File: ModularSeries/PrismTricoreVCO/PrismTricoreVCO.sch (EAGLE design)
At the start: 56 parts, among them IC1 LM13700_DIP, IC2 TL084P, IC3 TL084P, Q1 2N3906, Q2 2N3906

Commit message: Prism files added, readme updated
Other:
- note added: "Prism Triangle Core Voltage Controlled Oscillator Aidan Taylor 2020 ELECTRIC NOODLE BOX"
- note removed: "Triangle Core Voltage Controlled Oscillator Aidan Taylor 2020 ELECTRIC NOODLE BOX"
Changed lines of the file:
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@@
 <text x="81.28" y="139.7" size="1.778" layer="97" align="center">Q1 and Q2 are a matched to within 1.5mV Vbe
 and are in physical contact with R16</text>
-<text x="-45.72" y="22.86" size="2.54" layer="97" align="center-left">Triangle Core Voltage Controlled Oscillator
+<text x="-45.72" y="22.86" size="2.54" layer="97" align="center-left">Prism
+Triangle Core Voltage Controlled Oscillator
 Aidan Taylor 2020
 ELECTRIC NOODLE BOX</text>

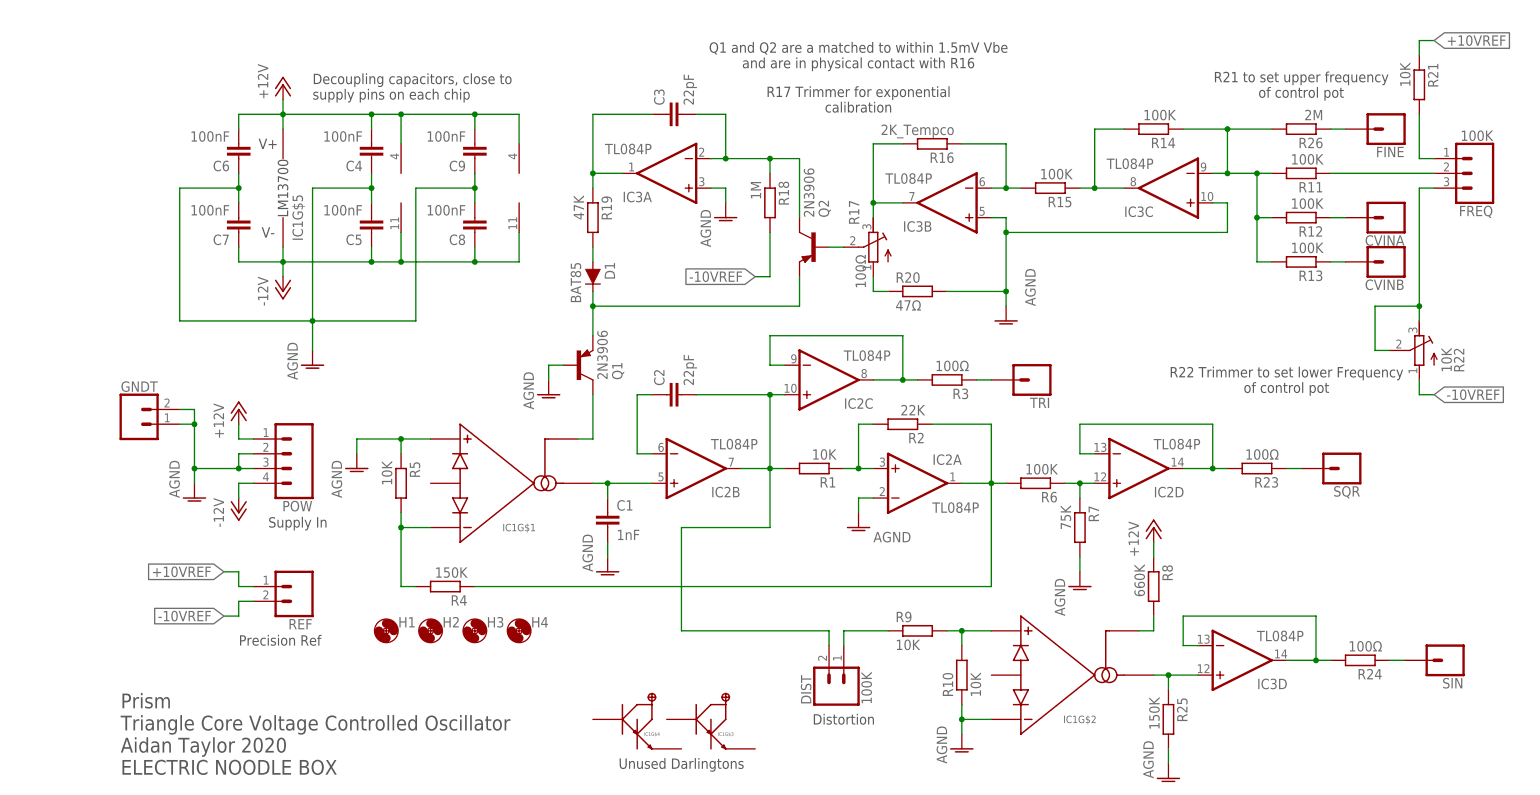
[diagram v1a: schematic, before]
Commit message: All PCBs now use unified library, Eagle library added
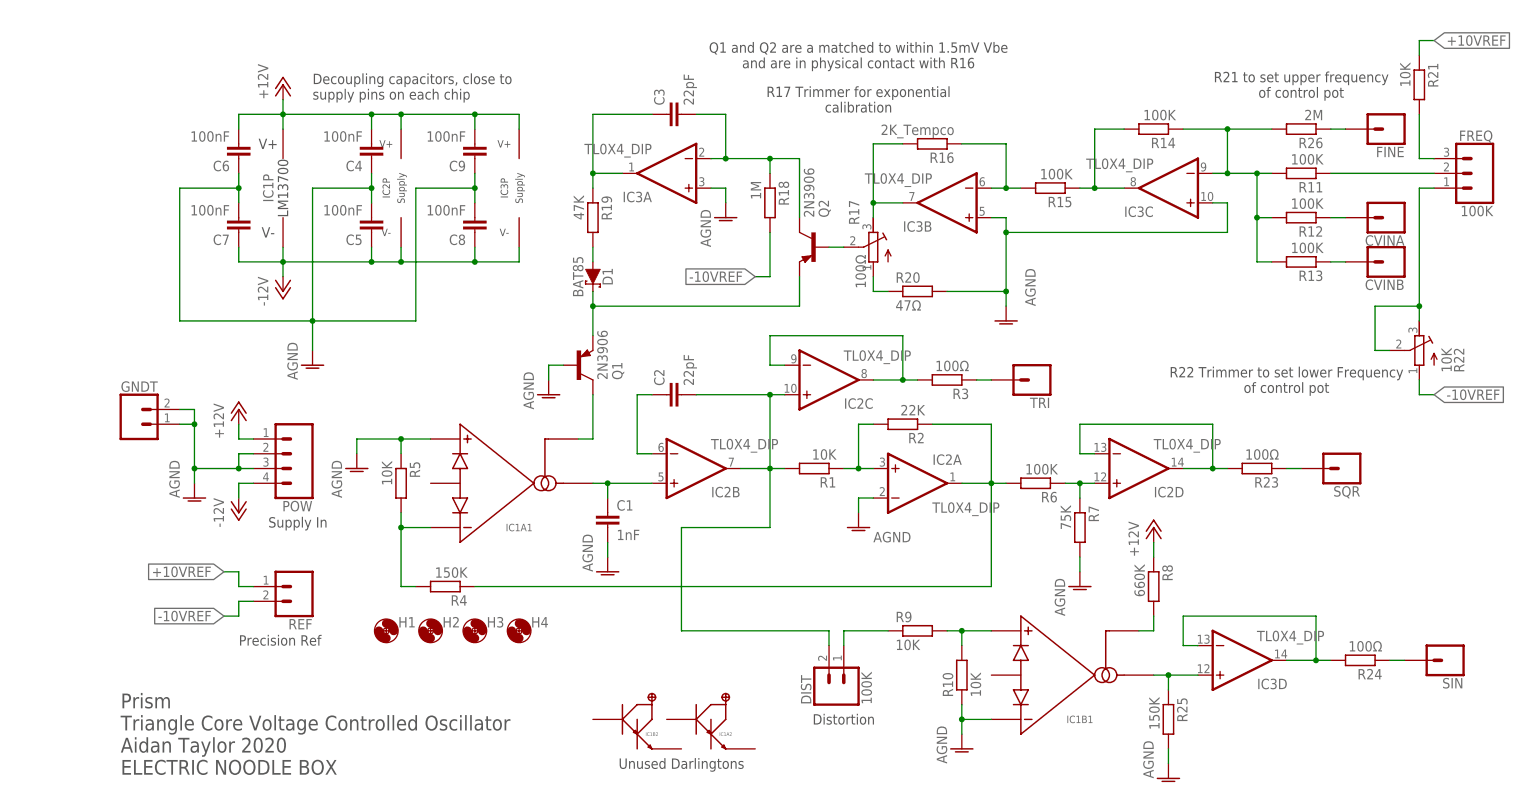
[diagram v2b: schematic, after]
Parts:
- CVINA, CVINB, FINE, SIN, SQR, TRI: value (none) -> 1XWIREPAD; device SparkFun-Connectors:CONN_01 -> ElectricNoodleBox:1XWIREPAD
- D1: device SparkFun-DiscreteSemi:DIODE-1N4148 -> ElectricNoodleBox:SCHOTTKY_DO35
- DIST: device SparkFun-Connectors:CONN_02 -> ElectricNoodleBox:2XWIREPAD
- FREQ: device SparkFun-Connectors:CONN_03 -> ElectricNoodleBox:3XWIREPAD
- GNDT: value (none) -> 2XWIREPAD; device SparkFun-Connectors:CONN_02 -> ElectricNoodleBox:2XWIREPAD
- IC1: device ElectricNoodleBox2018:LM13700_DIP -> ElectricNoodleBox:LM13700_DIP
- IC2, IC3: value TL084P -> TL0X4_DIP; device linear:TL084P -> ElectricNoodleBox:TL0X4_DIP
- POW: value (none) -> 4XMOLEX; device SparkFun-Connectors:CONN_04POLAR -> ElectricNoodleBox:4XMOLEX
- REF: value (none) -> 2XMOLEX; device SparkFun-Connectors:CONN_02POLAR -> ElectricNoodleBox:2XMOLEX
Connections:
- net +12V: now also IC1P.V+; no longer IC1G$5.V+
- net -12V: now also IC1P.V-; no longer IC1G$5.V-
- net AGND: now also IC1A1.AMP+, IC1B1.AMP-; no longer IC1G$1.AMP+, IC1G$2.AMP-
- net N$10: now also IC1B1.AMPOUT; no longer IC1G$2.AMPOUT
- net N$11: now also IC1B1.AMPBIAS; no longer IC1G$2.AMPBIAS
- net N$12: now also IC1A1.AMPBIAS; no longer IC1G$1.AMPBIAS
- net N$25: now also FREQ.1; no longer FREQ.3
- net N$26: now also FREQ.3; no longer FREQ.1
- net N$4: now also IC1A1.AMPOUT; no longer IC1G$1.AMPOUT
- net N$7: now also IC1A1.AMP-; no longer IC1G$1.AMP-
- net N$8: now also IC1B1.AMP+; no longer IC1G$2.AMP+

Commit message: C2 removed from Prism
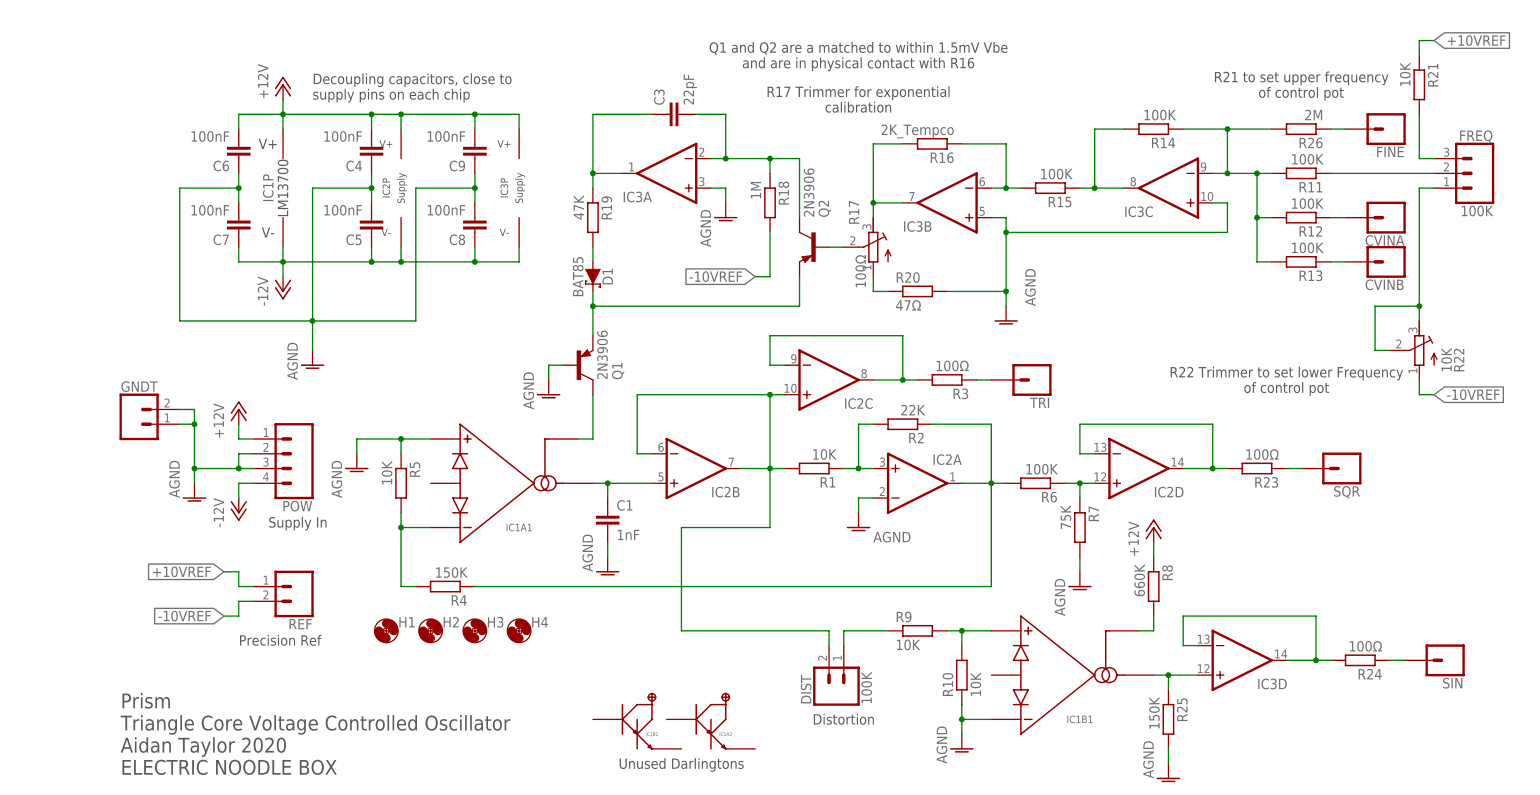
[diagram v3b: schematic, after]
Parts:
- removed C2: 22pF, rcl:C-EU050-025X075
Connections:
- removed net N$2: C2.2, DIST.2, IC2B.OUT, IC2C.+IN, R1.2
- net N$1: now also DIST.2, IC2B.OUT, IC2C.+IN, R1.2; no longer C2.1
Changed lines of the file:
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@@
 <part name="AGND1" library="supply1" library_urn="urn:adsk.eagle:library:371" deviceset="AGND" device=""/>
 <part name="AGND3" library="supply1" library_urn="urn:adsk.eagle:library:371" deviceset="AGND" device=""/>
-<part name="C2" library="rcl" library_urn="urn:adsk.eagle:library:334" deviceset="C-EU" device="050-025X075" package3d_urn="urn:adsk.eagle:package:23637/1" value="22pF"/>
 <part name="R2" library="rcl" library_urn="urn:adsk.eagle:library:334" deviceset="R-EU_" device="0207/10" package3d_urn="urn:adsk.eagle:package:23491/2" value="22K"/>
 <part name="R3" library="rcl" library_urn="urn:adsk.eagle:library:334" deviceset="R-EU_" device="0207/10" package3d_urn="urn:adsk.eagle:package:23491/2" value="100Ω"/>
@@
 <instance part="IC2" gate="B" x="53.34" y="68.58" smashed="yes" rot="MR180">
 <attribute name="NAME" x="55.88" y="65.405" size="1.778" layer="95" rot="MR180"/>
-<attribute name="VALUE" x="55.88" y="73.66" size="1.778" layer="96" rot="MR180"/>
 </instance>
 <instance part="IC2" gate="C" x="76.2" y="83.82" smashed="yes" rot="MR180">
 <attribute name="NAME" x="78.74" y="80.645" size="1.778" layer="95" rot="MR180"/>
-<attribute name="VALUE" x="78.74" y="88.9" size="1.778" layer="96" rot="MR180"/>
 </instance>
 <instance part="IC2" gate="A" x="91.44" y="66.04" smashed="yes">
 <attribute name="NAME" x="93.98" y="69.215" size="1.778" layer="95"/>
-<attribute name="VALUE" x="93.98" y="60.96" size="1.778" layer="96"/>
 </instance>
 <instance part="IC2" gate="D" x="129.54" y="68.58" smashed="yes" rot="MR180">
 <attribute name="NAME" x="132.08" y="65.405" size="1.778" layer="95" rot="MR180"/>
-<attribute name="VALUE" x="132.08" y="73.66" size="1.778" layer="96" rot="MR180"/>
 </instance>
 <instance part="IC2" gate="P" x="2.54" y="116.84" smashed="yes">
@@
 <attribute name="VALUE" x="83.82" y="55.88" size="1.778" layer="96"/>
 </instance>
-<instance part="C2" gate="G$1" x="48.26" y="81.28" smashed="yes" rot="R90">
-<attribute name="NAME" x="47.879" y="82.804" size="1.778" layer="95" rot="R90"/>
-<attribute name="VALUE" x="52.959" y="82.804" size="1.778" layer="96" rot="R90"/>
-</instance>
 <instance part="R2" gate="G$1" x="88.9" y="76.2" smashed="yes" rot="R180">
 <attribute name="NAME" x="92.71" y="74.7014" size="1.778" layer="95" rot="R180"/>
@@
 <instance part="IC3" gate="D" x="147.32" y="35.56" smashed="yes" rot="MR180">
 <attribute name="NAME" x="149.86" y="32.385" size="1.778" layer="95" rot="MR180"/>
-<attribute name="VALUE" x="149.86" y="40.64" size="1.778" layer="96" rot="MR180"/>
 </instance>
 <instance part="IC3" gate="C" x="134.62" y="116.84" smashed="yes" rot="R180">
 <attribute name="NAME" x="132.08" y="113.665" size="1.778" layer="95" rot="R180"/>
-<attribute name="VALUE" x="132.08" y="121.92" size="1.778" layer="96" rot="R180"/>
 </instance>
 <instance part="IC3" gate="B" x="96.52" y="114.3" smashed="yes" rot="R180">
 <attribute name="NAME" x="93.98" y="111.125" size="1.778" layer="95" rot="R180"/>
-<attribute name="VALUE" x="93.98" y="119.38" size="1.778" layer="96" rot="R180"/>
 </instance>
 <instance part="IC3" gate="A" x="48.26" y="119.38" smashed="yes" rot="R180">
 <attribute name="NAME" x="45.72" y="116.205" size="1.778" layer="95" rot="R180"/>
-<attribute name="VALUE" x="45.72" y="124.46" size="1.778" layer="96" rot="R180"/>
 </instance>
 <instance part="IC3" gate="P" x="22.86" y="116.84" smashed="yes">
@@
 <wire x1="45.72" y1="71.12" x2="43.18" y2="71.12" width="0.1524" layer="91"/>
 <wire x1="43.18" y1="71.12" x2="43.18" y2="81.28" width="0.1524" layer="91"/>
-<pinref part="C2" gate="G$1" pin="1"/>
-<wire x1="43.18" y1="81.28" x2="45.72" y2="81.28" width="0.1524" layer="91"/>
-</segment>
-</net>
-<net name="N$2" class="0">
-<segment>
-<pinref part="C2" gate="G$1" pin="2"/>
-<wire x1="53.34" y1="81.28" x2="66.04" y2="81.28" width="0.1524" layer="91"/>
+<wire x1="43.18" y1="81.28" x2="66.04" y2="81.28" width="0.1524" layer="91"/>
 <wire x1="66.04" y1="81.28" x2="66.04" y2="68.58" width="0.1524" layer="91"/>
 <pinref part="IC2" gate="B" pin="OUT"/>

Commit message: Library updated, variants consolidated
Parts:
- IC1: value LM13700_DIP -> (none); device ElectricNoodleBox:LM13700_DIP -> ElectricNoodleBox:LM13700DIL
- IC2, IC3: value TL0X4_DIP -> (none); device ElectricNoodleBox:TL0X4_DIP -> ElectricNoodleBox:TL0X4DIL
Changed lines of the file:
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@@
 </classes>
 <parts>
-<part name="IC1" library="ElectricNoodleBox" deviceset="LM13700_DIP" device="" package3d_urn="urn:adsk.eagle:package:922/2"/>
-<part name="IC2" library="ElectricNoodleBox" deviceset="TL0X4_DIP" device="" package3d_urn="urn:adsk.eagle:package:16407/2"/>
+<part name="IC1" library="ElectricNoodleBox" deviceset="LM13700" device="DIL" package3d_urn="urn:adsk.eagle:package:922/2"/>
+<part name="IC2" library="ElectricNoodleBox" deviceset="TL0X4" device="DIL" package3d_urn="urn:adsk.eagle:package:16407/2"/>
 <part name="R1" library="rcl" library_urn="urn:adsk.eagle:library:334" deviceset="R-EU_" device="0207/10" package3d_urn="urn:adsk.eagle:package:23491/2" value="10K"/>
 <part name="C1" library="rcl" library_urn="urn:adsk.eagle:library:334" deviceset="C-EU" device="050-025X075" package3d_urn="urn:adsk.eagle:package:23637/1" value="1nF"/>
@@
 <part name="AGND2" library="supply1" library_urn="urn:adsk.eagle:library:371" deviceset="AGND" device=""/>
 <part name="P+1" library="supply1" library_urn="urn:adsk.eagle:library:371" deviceset="+12V" device=""/>
-<part name="IC3" library="ElectricNoodleBox" deviceset="TL0X4_DIP" device="" package3d_urn="urn:adsk.eagle:package:16407/2"/>
+<part name="IC3" library="ElectricNoodleBox" deviceset="TL0X4" device="DIL" package3d_urn="urn:adsk.eagle:package:16407/2"/>
 <part name="R11" library="rcl" library_urn="urn:adsk.eagle:library:334" deviceset="R-EU_" device="0207/10" package3d_urn="urn:adsk.eagle:package:23491/2" value="100K"/>
 <part name="R12" library="rcl" library_urn="urn:adsk.eagle:library:334" deviceset="R-EU_" device="0207/10" package3d_urn="urn:adsk.eagle:package:23491/2" value="100K"/>

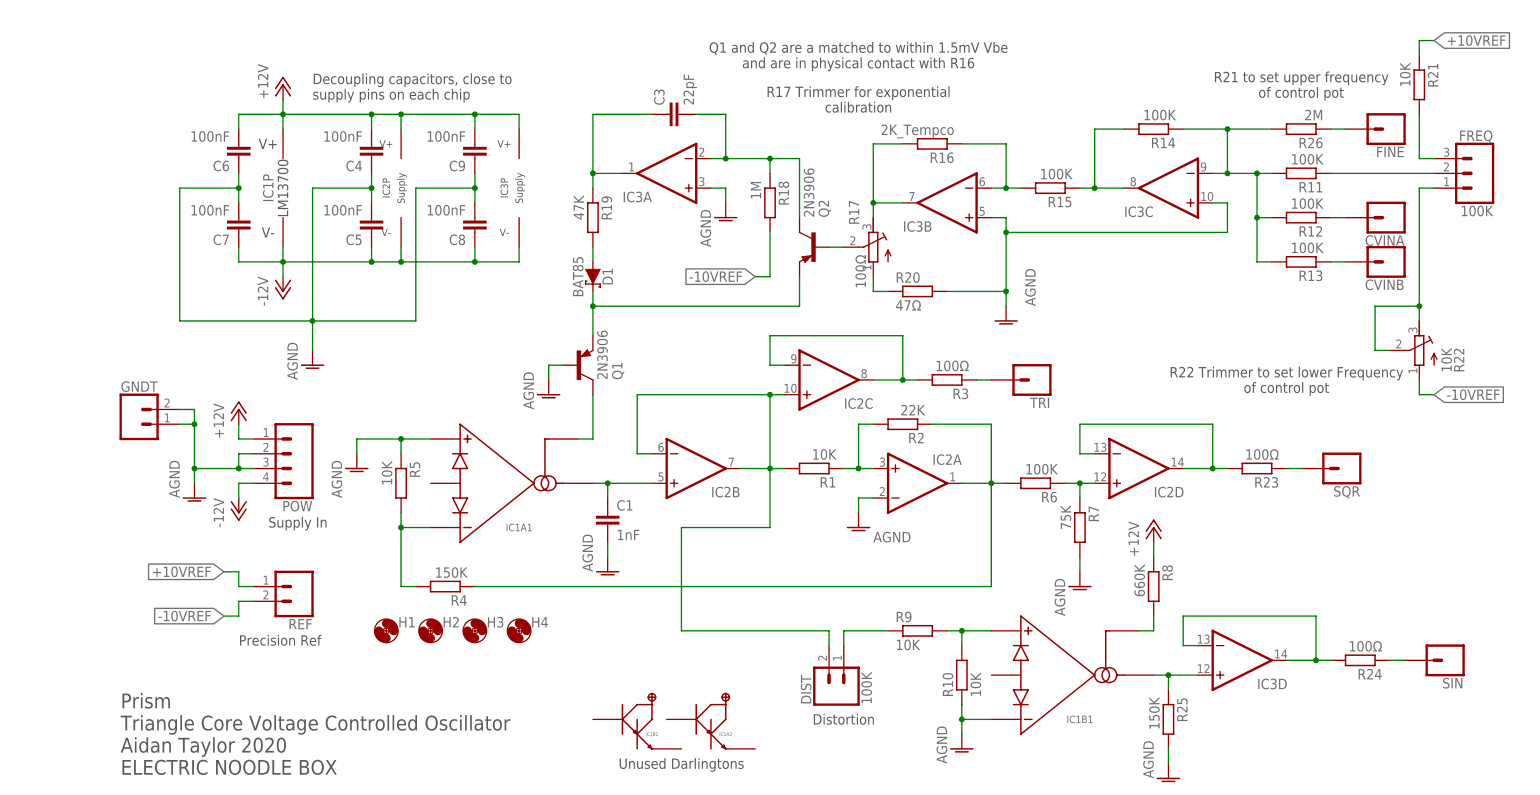
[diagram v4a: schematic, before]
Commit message: Power header updated on most PCBs. Knives layout added
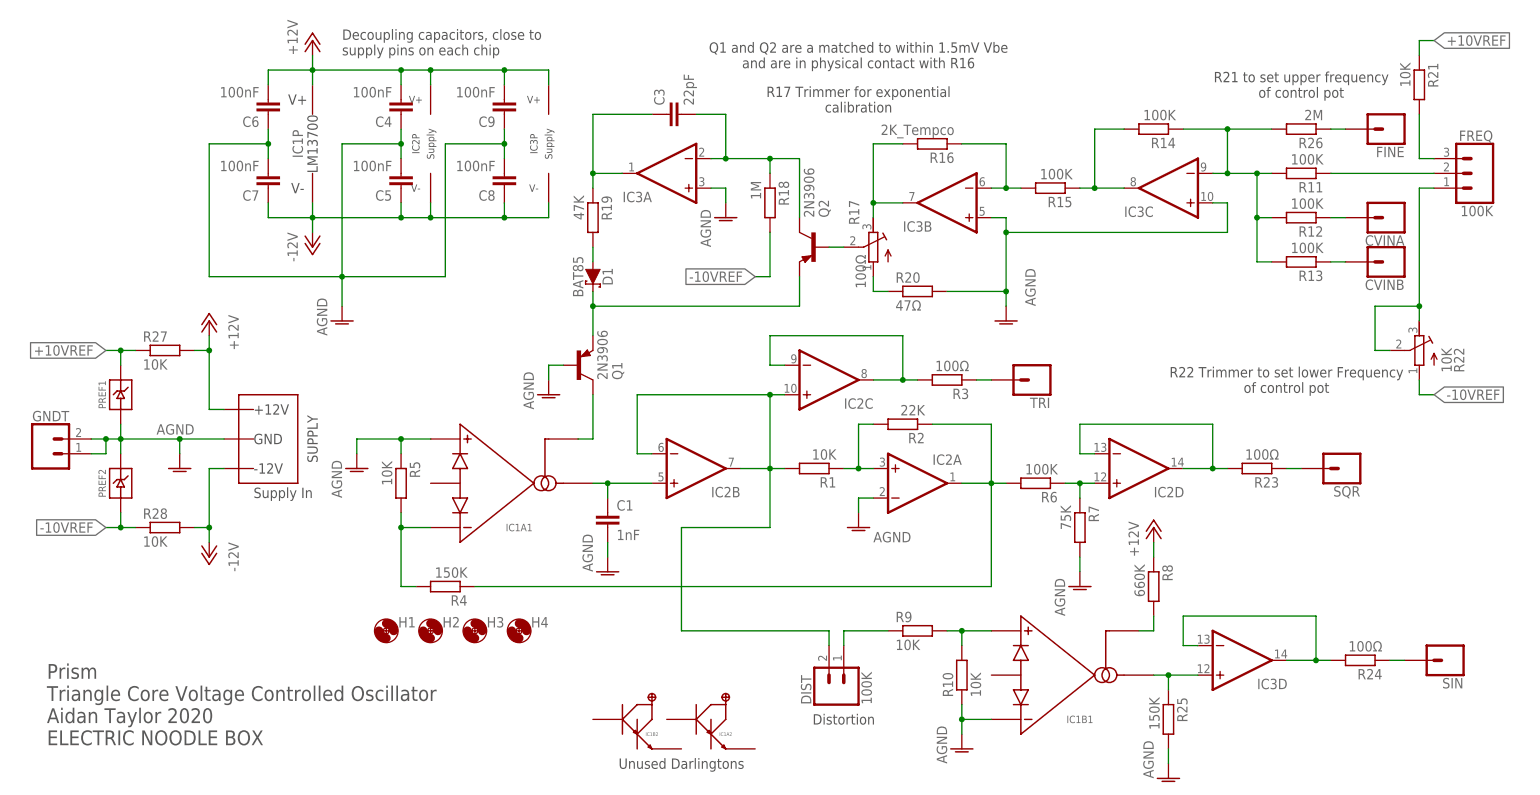
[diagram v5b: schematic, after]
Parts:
- removed POW: 4XMOLEX, ElectricNoodleBox:4XMOLEX
- removed REF: 2XMOLEX, ElectricNoodleBox:2XMOLEX
- added PREF1, PREF2: (no value), ElectricNoodleBox:LM4040TH
- added R27, R28: 10K, rcl:R-EU_0207/10
- added WP1: COMBO_SUPPLY_HEADER, ElectricNoodleBox:COMBO_SUPPLY_HEADER
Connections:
- net +10VREF: now also PREF1.CATHODE, R27.1; no longer REF.1
- net +12V: now also R27.2, WP1.V++; no longer POW.1
- net -10VREF: now also PREF2.ANODE, R28.1; no longer REF.2
- net -12V: now also R28.2, WP1.V--; no longer POW.4
- net AGND: now also PREF1.ANODE, PREF2.CATHODE, WP1.AGND; no longer POW.2, POW.3
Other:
- note removed: "Precision Ref"
- moved on the sheet: C4, C5, C6, C7, C8, C9, GNDT, IC1P, IC2P, IC3P
